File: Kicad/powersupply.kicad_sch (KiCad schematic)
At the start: 25 parts, among them J1101 Jack 2.1{slash}6.3mm, J1102 2x2 Socket, J1103 4-pin Socket, Q1101 BC546, Q1102 AO3401A, Q1103 BC556, U1101 DC-DC Module, U1102 HT7533-1-SOT89, U1103 AMS1117-3.3

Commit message: Set DAC to 1k/2k. Closes #77 Replaced some CPL resistors. Partial fix for #83 Added bridges for VGA I2C if ESD chip not fitted. Closes #51
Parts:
- R1101, R1102, R1103, R1104: Digikey (none) -> RMCF0805FT10K0CT-ND; MPN CPL-RES-0805-10K-0.125W -> RMCF0805FT10K0; Manufacturer CPL -> Stackpole
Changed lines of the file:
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@@
       (effects (font (size 1.27 1.27)) hide)
     )
-    (property "Digikey" "~" (id 5) (at 76.2 156.845 0)
-      (effects (font (size 1.27 1.27)) hide)
-    )
-    (property "MPN" "CPL-RES-0805-10K-0.125W" (id 6) (at 76.2 156.845 0)
-      (effects (font (size 1.27 1.27)) hide)
-    )
-    (property "Manufacturer" "CPL" (id 7) (at 76.2 156.845 0)
+    (property "Digikey" "RMCF0805FT10K0CT-ND" (id 5) (at 76.2 156.845 0)
+      (effects (font (size 1.27 1.27)) hide)
+    )
+    (property "MPN" "RMCF0805FT10K0" (id 6) (at 76.2 156.845 0)
+      (effects (font (size 1.27 1.27)) hide)
+    )
+    (property "Manufacturer" "Stackpole" (id 7) (at 76.2 156.845 0)
       (effects (font (size 1.27 1.27)) hide)
     )
@@
       (effects (font (size 1.27 1.27)) hide)
     )
-    (property "Digikey" "~" (id 5) (at 60.325 141.605 0)
-      (effects (font (size 1.27 1.27)) hide)
-    )
-    (property "MPN" "CPL-RES-0805-10K-0.125W" (id 6) (at 60.325 141.605 0)
-      (effects (font (size 1.27 1.27)) hide)
-    )
-    (property "Manufacturer" "CPL" (id 7) (at 60.325 141.605 0)
+    (property "Digikey" "RMCF0805FT10K0CT-ND" (id 5) (at 60.325 141.605 0)
+      (effects (font (size 1.27 1.27)) hide)
+    )
+    (property "MPN" "RMCF0805FT10K0" (id 6) (at 60.325 141.605 0)
+      (effects (font (size 1.27 1.27)) hide)
+    )
+    (property "Manufacturer" "Stackpole" (id 7) (at 60.325 141.605 0)
       (effects (font (size 1.27 1.27)) hide)
     )
@@
       (effects (font (size 1.27 1.27)) hide)
     )
-    (property "Digikey" "~" (id 5) (at 38.735 150.495 0)
-      (effects (font (size 1.27 1.27)) hide)
-    )
-    (property "MPN" "CPL-RES-0805-10K-0.125W" (id 6) (at 38.735 150.495 0)
-      (effects (font (size 1.27 1.27)) hide)
-    )
-    (property "Manufacturer" "CPL" (id 7) (at 38.735 150.495 0)
+    (property "Digikey" "RMCF0805FT10K0CT-ND" (id 5) (at 38.735 150.495 0)
+      (effects (font (size 1.27 1.27)) hide)
+    )
+    (property "MPN" "RMCF0805FT10K0" (id 6) (at 38.735 150.495 0)
+      (effects (font (size 1.27 1.27)) hide)
+    )
+    (property "Manufacturer" "Stackpole" (id 7) (at 38.735 150.495 0)
       (effects (font (size 1.27 1.27)) hide)
     )
@@
       (effects (font (size 1.27 1.27)) hide)
     )
-    (property "Digikey" "~" (id 5) (at 60.96 70.485 0)
-      (effects (font (size 1.27 1.27)) hide)
-    )
-    (property "MPN" "CPL-RES-0805-10K-0.125W" (id 6) (at 60.96 70.485 0)
-      (effects (font (size 1.27 1.27)) hide)
-    )
-    (property "Manufacturer" "CPL" (id 7) (at 60.96 70.485 0)
-      (effects (font (size 1.27 1.27)) hide)
-    )
+    (property "Digikey" "RMCF0805FT10K0CT-ND" (id 5) (at 60.96 70.485 0)
+      (effects (font (size 1.27 1.27)) hide)
+    )
+    (property "MPN" "RMCF0805FT10K0" (id 6) (at 60.96 70.485 0)
+      (effects (font (size 1.27 1.27)) hide)
+    )
+    (property "Manufacturer" "Stackpole" (id 7) (at 60.96 70.485 0)
+      (effects (font (size 1.27 1.27)) hide)
+    )

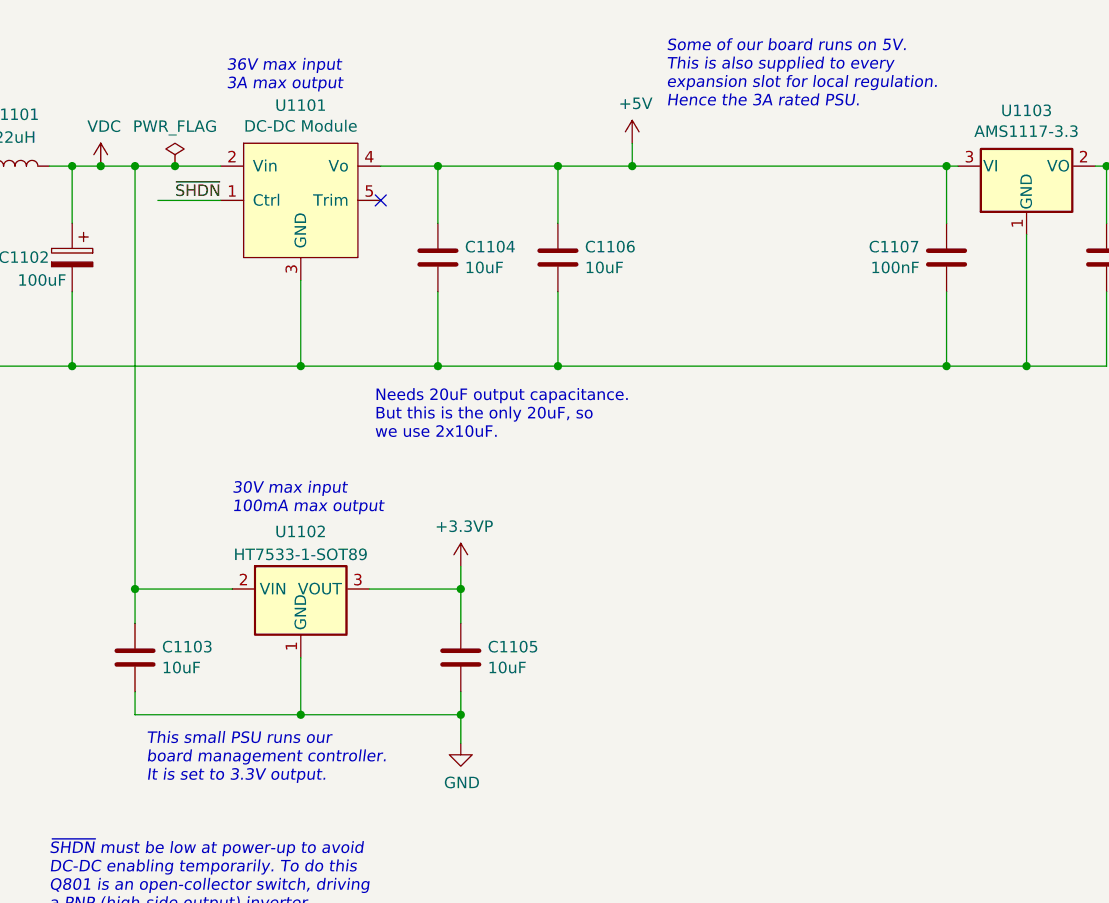
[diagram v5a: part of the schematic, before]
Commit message: Removed all CPL parts, and changed standby PSU.
The Holtek was a SOT-89 that had a completely different pinout to
every other SOT-89 3.3V LDO out there. To avoid confusion I
wanted to replace it, but the only other basic JLCPCB parts
were the AMS1117 (huge quiescent current) and something only
rated to 7V input voltage (this LDO gets the full VDC in).

So, I used a TO-92 footprint and picked an LP2950N.

This, however, needs some ESR on the output cap, so I made
that a 2.2uF electrolytic.

I also removed the 2x 10uF output caps on the K7805 and set
just one 22uF as specified in the datasheet.
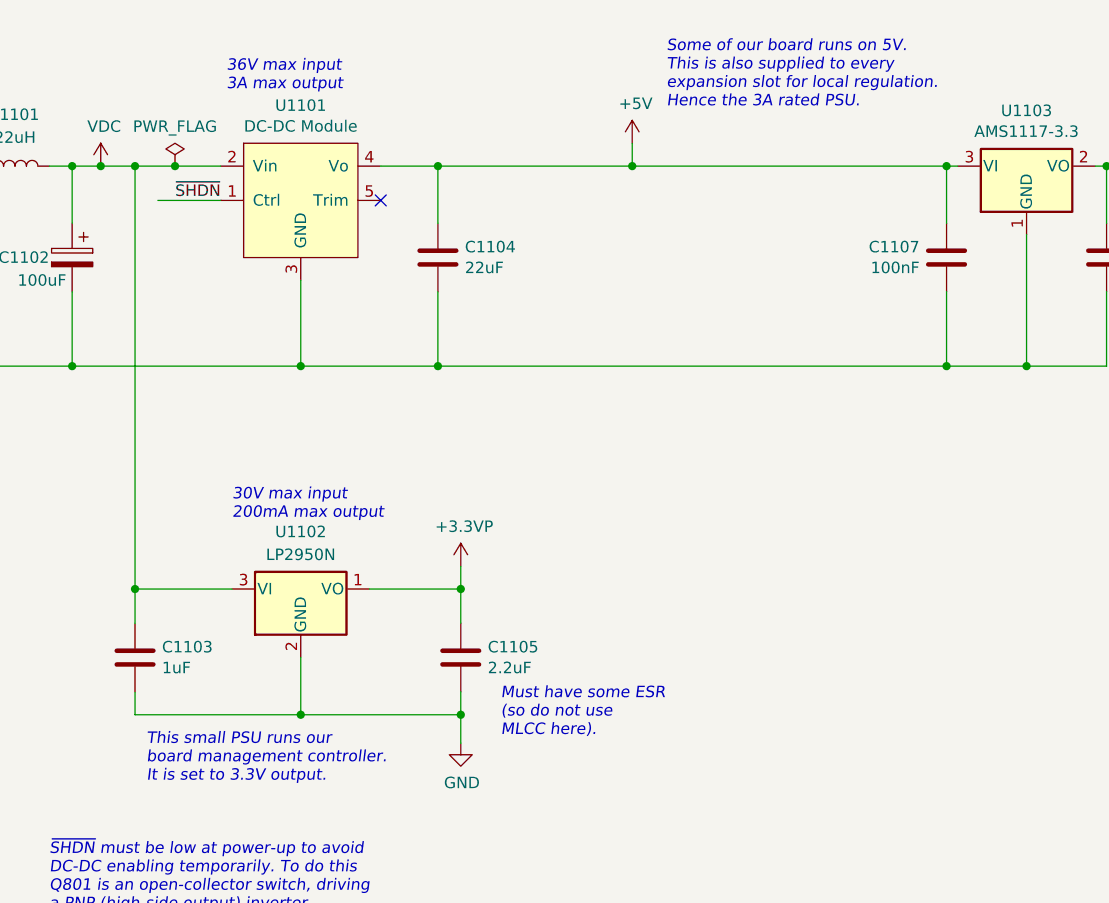
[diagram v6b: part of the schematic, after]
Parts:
- removed C1106: 10uF, Capacitor_SMD:C_0805_2012Metric_Pad1.18x1.45mm_HandSolder, symbol Device:C
- C1101, C1102: Digikey (none) -> P5182-ND; MPN CPL-CAP-ALU-RAD-100UF-50V -> ECA-1HM101; Manufacturer CPL -> Panasonic; Mouser (none) -> 667-ECA-1HM101
- C1103: value 10uF -> 1uF; Digikey (none) -> 311-1456-1-ND; LCSC Part# C15850 -> C28323; MPN CPL-CAP-X5R-0805-10UF-16V -> CC0805KKX7R8BB105; Manufacturer CPL -> Yageo; Mouser (none) -> 603-CC805KKX7R8BB105; Voltage 16V -> 25V
- C1104: value 10uF -> 22uF; Digikey (none) -> 490-3886-1-ND; LCSC Part# C15850 -> C602037; MPN CPL-CAP-X5R-0805-10UF-16V -> CL21A226MAYNNNE; Manufacturer CPL -> Samsung; Mouser (none) -> 187-CL21A226MAYNNNE
- C1105: value 10uF -> 2.2uF; footprint Capacitor_SMD:C_0805_2012Metric_Pad1.18x1.45mm_HandSolder -> Capacitor_SMD:CP_Elec_4x5.4; Digikey (none) -> PCE4027CT-ND; LCSC Part# C15850 -> C72492; MPN CPL-CAP-X5R-0805-10UF-16V -> EEE-FC1V2R2R; Manufacturer CPL -> Panasonic; Mouser (none) -> 667-EEE-FC1V2R2R; Tolerance X5R -> 20%; Voltage 16V -> 10V
- C1107: Digikey (none) -> 399-C0805C104M5RAC7800CT-ND; MPN CPL-CAP-X7R-0805-100NF-50V -> C0805C104M5RACTU; Manufacturer CPL -> Kemet; Mouser (none) -> 80-C0805C104M5R
- C1108: Digikey (none) -> 490-3886-1-ND; MPN CPL-CAP-X5R-0805-10UF-16V -> GRM21BR61C106KE15L; Manufacturer CPL -> Murata; Mouser (none) -> 81-GRM21BR61C106KE15
- U1102: value HT7533-1-SOT89 -> LP2950N; footprint Package_TO_SOT_SMD:SOT-89-3 -> Package_TO_SOT_THT:TO-92_Inline; symbol Regulator_Linear:HT75xx-1-SOT89 -> Regulator_Linear:LP2950-3.3_TO92; Digikey (none) -> 296-26120-ND; LCSC Part# C14289 -> (none); MPN (none) -> LP2950-33LPE3; Manufacturer (none) -> Texas Instruments; Mouser (none) -> 595-LP2950-33LPE3
- U1103: Digikey (none) -> NCP1117ST33T3GOSCT-ND; MPN CPL-REG-LIN-3.3V-1A -> NCP1117ST33T3GOS; Manufacturer CPL -> ON Semiconductor; Mouser (none) -> 863-NCP1117ST33T3G
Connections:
- net +3.3VP: now also U1102.1 (VO); no longer U1102.3 (VOUT)
- net GND: now also U1102.2 (GND); no longer U1102.1 (GND)
- net VDC: now also U1102.3 (VI); no longer U1102.2 (VIN)
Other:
- note added: "30V max input 200mA max output"
- note added: "Must have some ESR (so do not use MLCC here)."
- note removed: "30V max input 100mA max output"
- note removed: "Needs 20uF output capacitance. But this is the only 20uF, so we use 2x10uF."

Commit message: LED and Switch updates.
Case LEDs are now driven by VDC and 1K. Allows higher Vf LEDs to work.
Added 6mm buttons.
Fiddled with tracking around CODEC.
Change I2S pin ordering.

Closes: #42 #60 #46
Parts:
- renumbered C1107 to C1106, C1108 to C1107
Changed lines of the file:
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@@
   (symbol (lib_id "Device:C") (at 191.77 64.135 0) (mirror y) (unit 1)
     (in_bom yes) (on_board yes)
-    (property "Reference" "C1107" (id 0) (at 188.7728 62.9666 0)
+    (property "Reference" "C1106" (id 0) (at 188.7728 62.9666 0)
       (effects (font (size 1.27 1.27)) (justify left))
     )
@@
   (symbol (lib_id "Device:C") (at 209.55 64.135 0) (unit 1)
     (in_bom yes) (on_board yes)
-    (property "Reference" "C1108" (id 0) (at 212.5472 62.9666 0)
-      (effects (font (size 1.27 1.27)) (justify left))
-    )
+    (property "Reference" "C1107" (id 0) (at 212.5472 62.9666 0)
+      (effects (font (size 1.27 1.27)) (justify left))
+    )

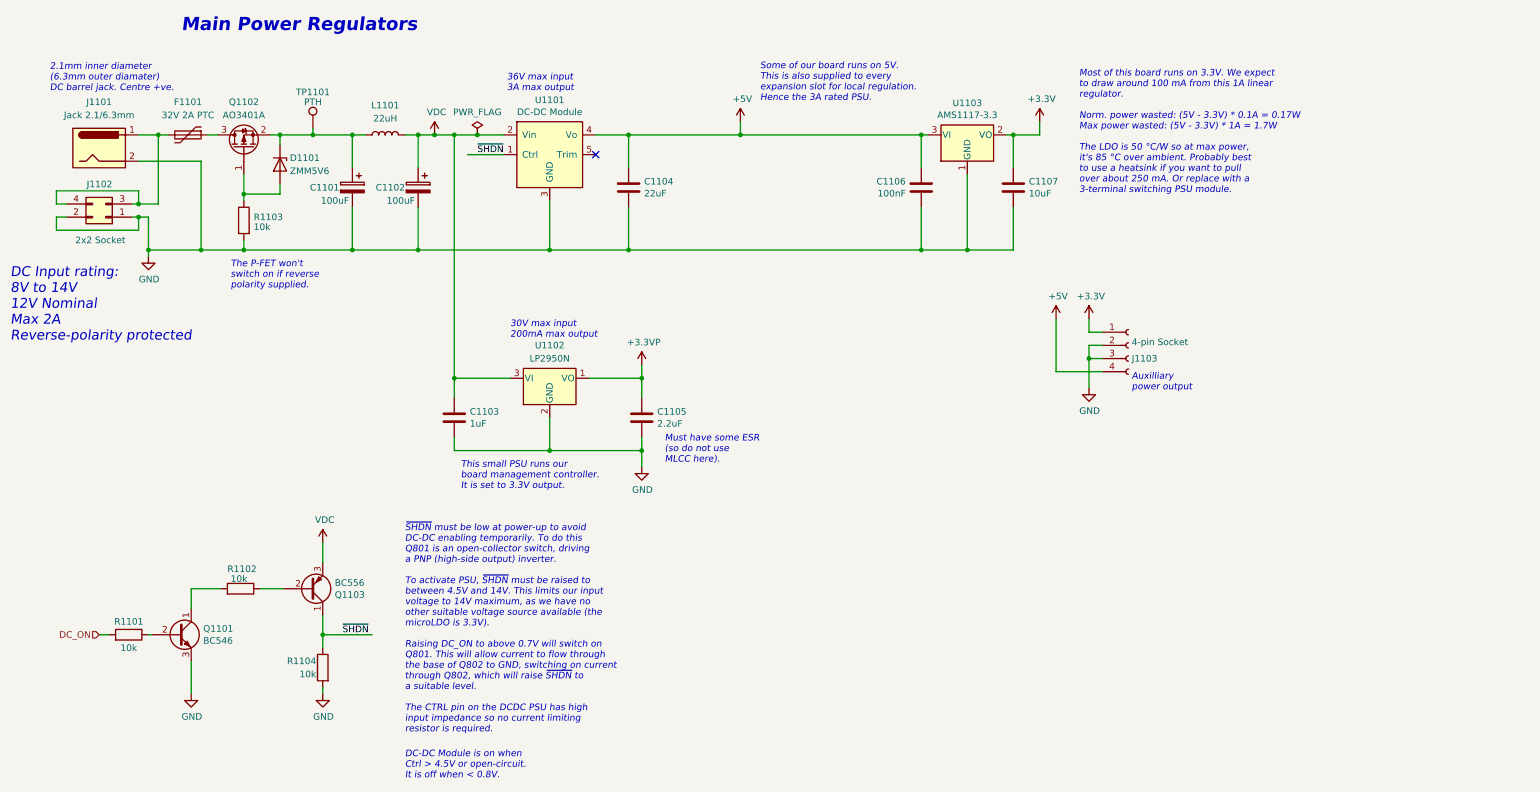
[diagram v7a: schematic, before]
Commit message: Changed LEDs to have NFET drivers. Moved power output header. Change TO-92 BJTs to SOT-23.
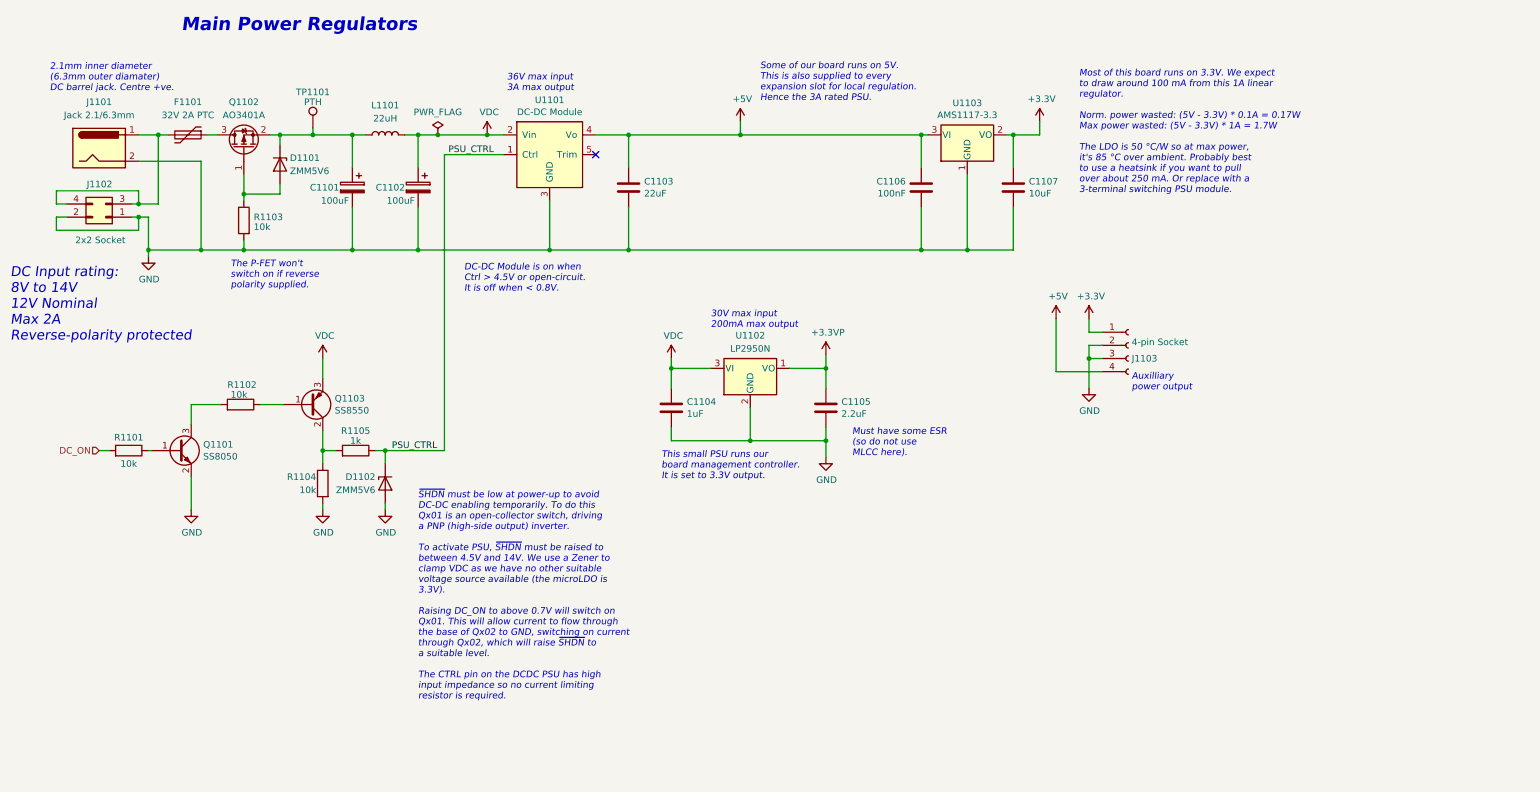
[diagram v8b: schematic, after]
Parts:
- added D1102: ZMM5V6, Diode_SMD:D_MiniMELF, symbol Diode:ZMMxx
- added R1105: 1k, Resistor_SMD:R_0805_2012Metric_Pad1.20x1.40mm_HandSolder, symbol Device:R
- Q1101: value BC546 -> SS8050; footprint Package_TO_SOT_THT:TO-92_Inline -> Package_TO_SOT_SMD:SOT-23; symbol Transistor_BJT:BC546 -> Transistor_BJT:S8050; Digikey BC546CTACT-ND -> MMSS8050-L-TPMSCT-ND; LCSC Part# (none) -> C105432; MPN BC546CTA -> S8050; Manufacturer ON Semiconductor -> JCET; Mouser 512-BC546CTA -> (none)
- Q1103: value BC556 -> SS8550; footprint Package_TO_SOT_THT:TO-92_Inline -> Package_TO_SOT_SMD:SOT-23; Digikey BC556BTFCT-ND -> MMSS8550-L-TPMSCT-ND; LCSC Part# (none) -> C8542; MPN BC556BTF -> SS8550; Manufacturer ON Semiconductor -> JCET; Mouser 512-BC556BTF -> (none)
- renumbered C1104 to C1103, C1103 to C1104
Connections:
- net GND: now also Q1101.2 (E), D1102.2 (A); no longer Q1101.3 (E)
- net at Q1101.1 (B): now also R1101.1; no longer R1102.2
- net at Q1103.2 (C): now also R1104.1, R1105.2; no longer R1102.1
- removed net ~{SHDN}: Q1103.1 (C), R1104.1, U1101.1 (Ctrl)
- new net: Q1101.3 (C), R1102.2
- new net: Q1103.1 (B), R1102.1
- new net PSU_CTRL: D1102.1 (K), R1105.1, U1101.1 (Ctrl)
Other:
- note added: "~{SHDN} must be low at power-up to avoid DC-DC enabling temporarily. To do this Qx01 is an open-collector switch, driving a PNP (high-side output) inverter. To activate PSU, ~{SHDN} must be raised to between 4.5V and 14V. We use a Zener to clamp VDC as we have no other suitable voltage source available (the microLDO is 3.3V). Raising DC_ON to above 0.7V will switch on Qx01. This will allow curren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"
- note removed: "~{SHDN} must be low at power-up to avoid DC-DC enabling temporarily. To do this Q801 is an open-collector switch, driving a PNP (high-side output) inverter. To activate PSU, ~{SHDN} must be raised to between 4.5V and 14V. This limits our input voltage to 14V maximum, as we have no other suitable voltage source available (the microLDO is 3.3V). Raising DC_ON to above 0.7V will switch on Q801. This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"
- moved on the sheet: C1104, C1105, Q1101, Q1103, R1101, R1102, R1104, U1102
